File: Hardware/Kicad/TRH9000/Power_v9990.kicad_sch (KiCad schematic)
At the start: 21 parts, among them U1 V9990, U2 KM428C256, U3 KM428C256, U4 74VHC138, U6 LMH1980, U7 T.I_SN74AHCT32D

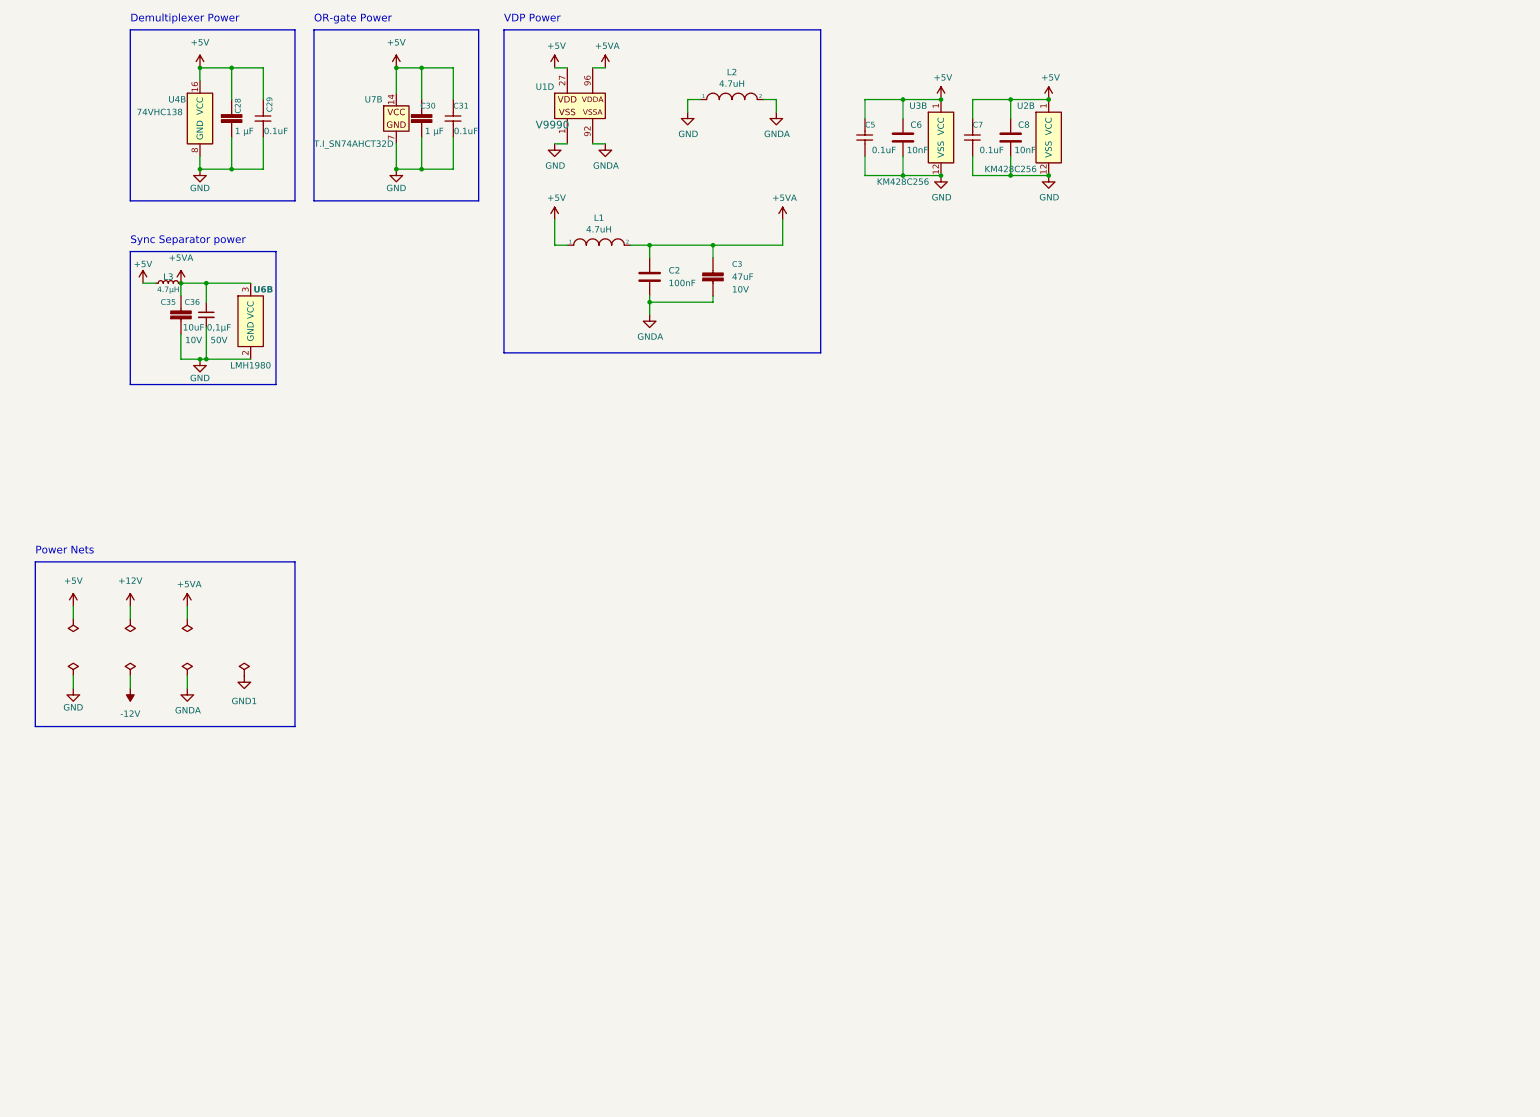
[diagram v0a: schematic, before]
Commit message: Started routing the PCB, adding cut-outs to separate the analog from digital signal-domains.
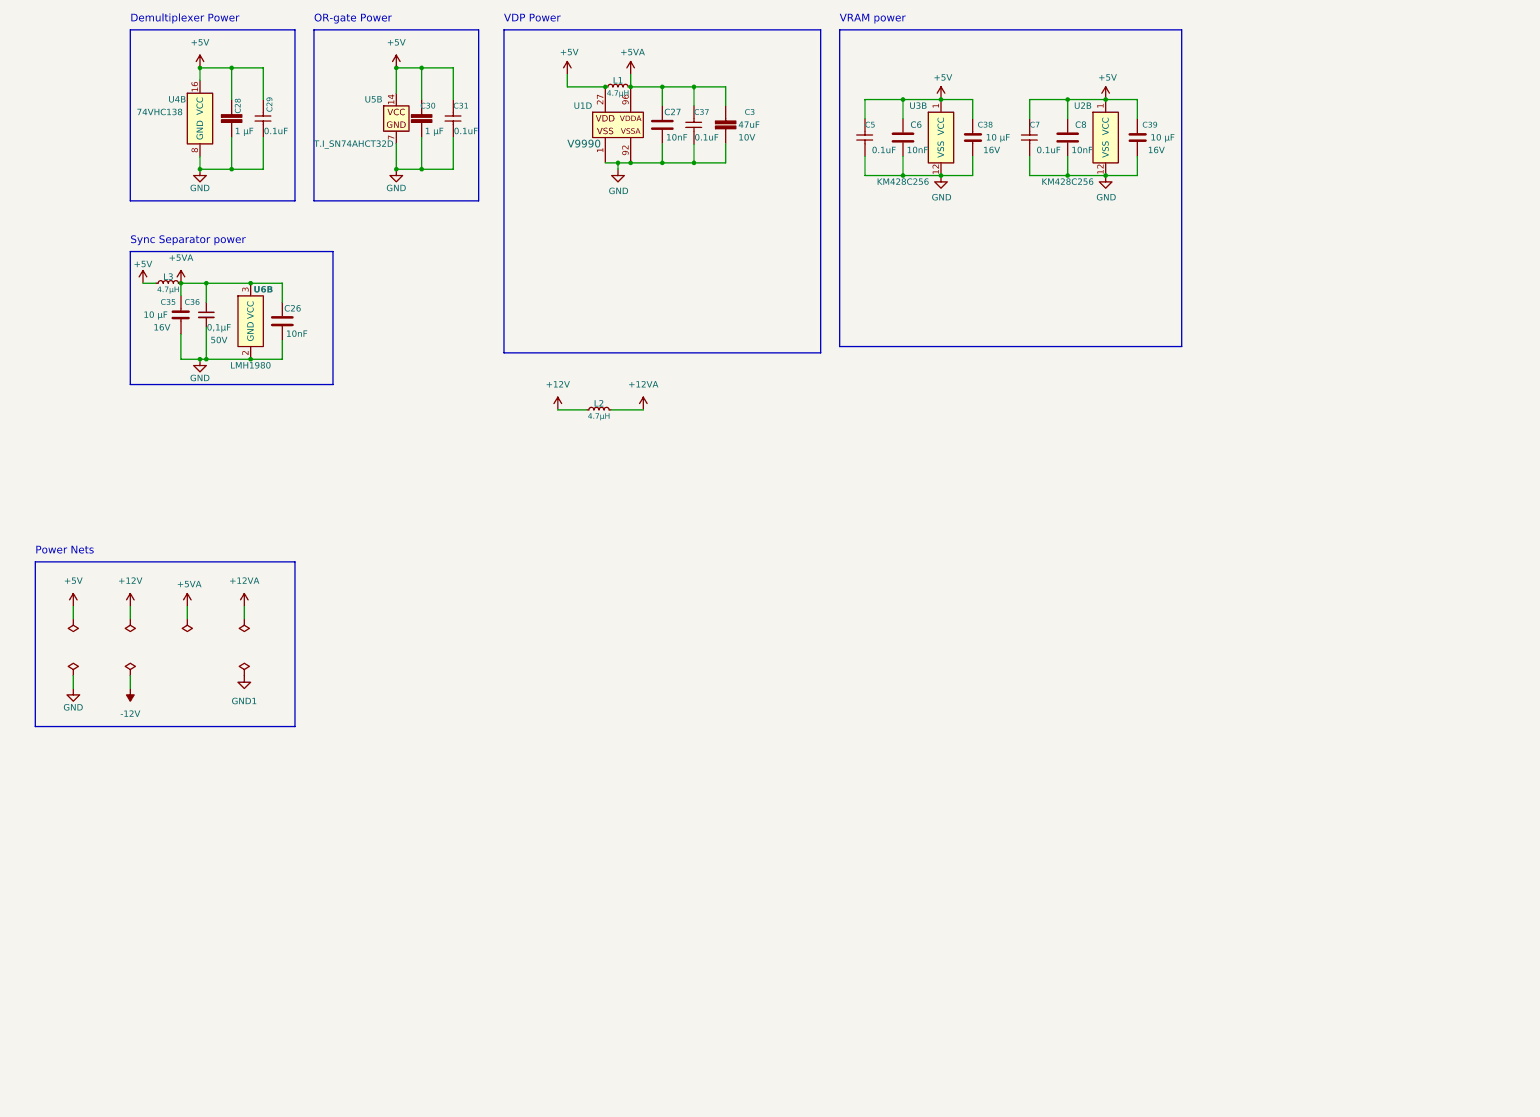
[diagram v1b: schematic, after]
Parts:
- removed C2: 100nF, Capacitor_SMD:C_0805_2012Metric, symbol Device:C
- removed L1, L2: 4.7uH, Inductor_SMD:L_1206_3216Metric, symbol pspice:INDUCTOR
- added C26, C27: 10nF, Capacitor_SMD:C_0805_2012Metric, symbol Device:C
- added C37: C_CC0805JPX7R9BB104, Capacitor_SMD:C_0805_2012Metric, symbol LRJ-parts:C_CC0805JPX7R9BB104
- added C38, C39: C_CL21B106KOQNNNE, Capacitor_SMD:C_0805_2012Metric, symbol LRJ-parts:C_CL21B106KOQNNNE
- added L1, L2: L_MLZ2012M4R7HT000, Inductor_SMD:L_0805_2012Metric, symbol LRJ-parts:L_MLZ2012M4R7HT000
- C35: value C_GRM21BR71A106KA73K -> C_CL21B106KOQNNNE; footprint Capacitor_SMD:C_0805_2012Metric_Pad1.18x1.45mm_HandSolder -> Capacitor_SMD:C_0805_2012Metric; symbol LRJ-parts:C_GRM21BR71A106KA73K -> LRJ-parts:C_CL21B106KOQNNNE;  Temperature Coefficient  X7R -> (none); Capacitance 10uF -> 10 µF; MPN GRM21BR71A106KA73K -> CL21B106KOQNNNE; Manufacturer Murata Electronics -> Samsung Electro-Mechanics; Mounting type (none) -> SMD; Status (none) -> Active; Temperature Coefficient  (none) -> X7R; Tolerance ±10% -> (none); Voltage rating 10V -> 16V
- renumbered U7 to U5
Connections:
- net GNDA is gone; now on net GND: C3.2, U1.92 (VSSA)
- net +12V: now also L2.1
- net +5V: now also C38.1, C39.1, L1.1
- net +5VA: now also C26.2, C27.2, C37.1, L1.2
- net GND: now also C26.1, C27.1, C37.2, C38.2, C39.2
- new net +12VA: L2.2
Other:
- note added: "VRAM power"
- moved on the sheet: C3, C7, C8, U1D, U2B

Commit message: More routing of the analog portion. Added 3D-models for the VGA and Scart connectors.
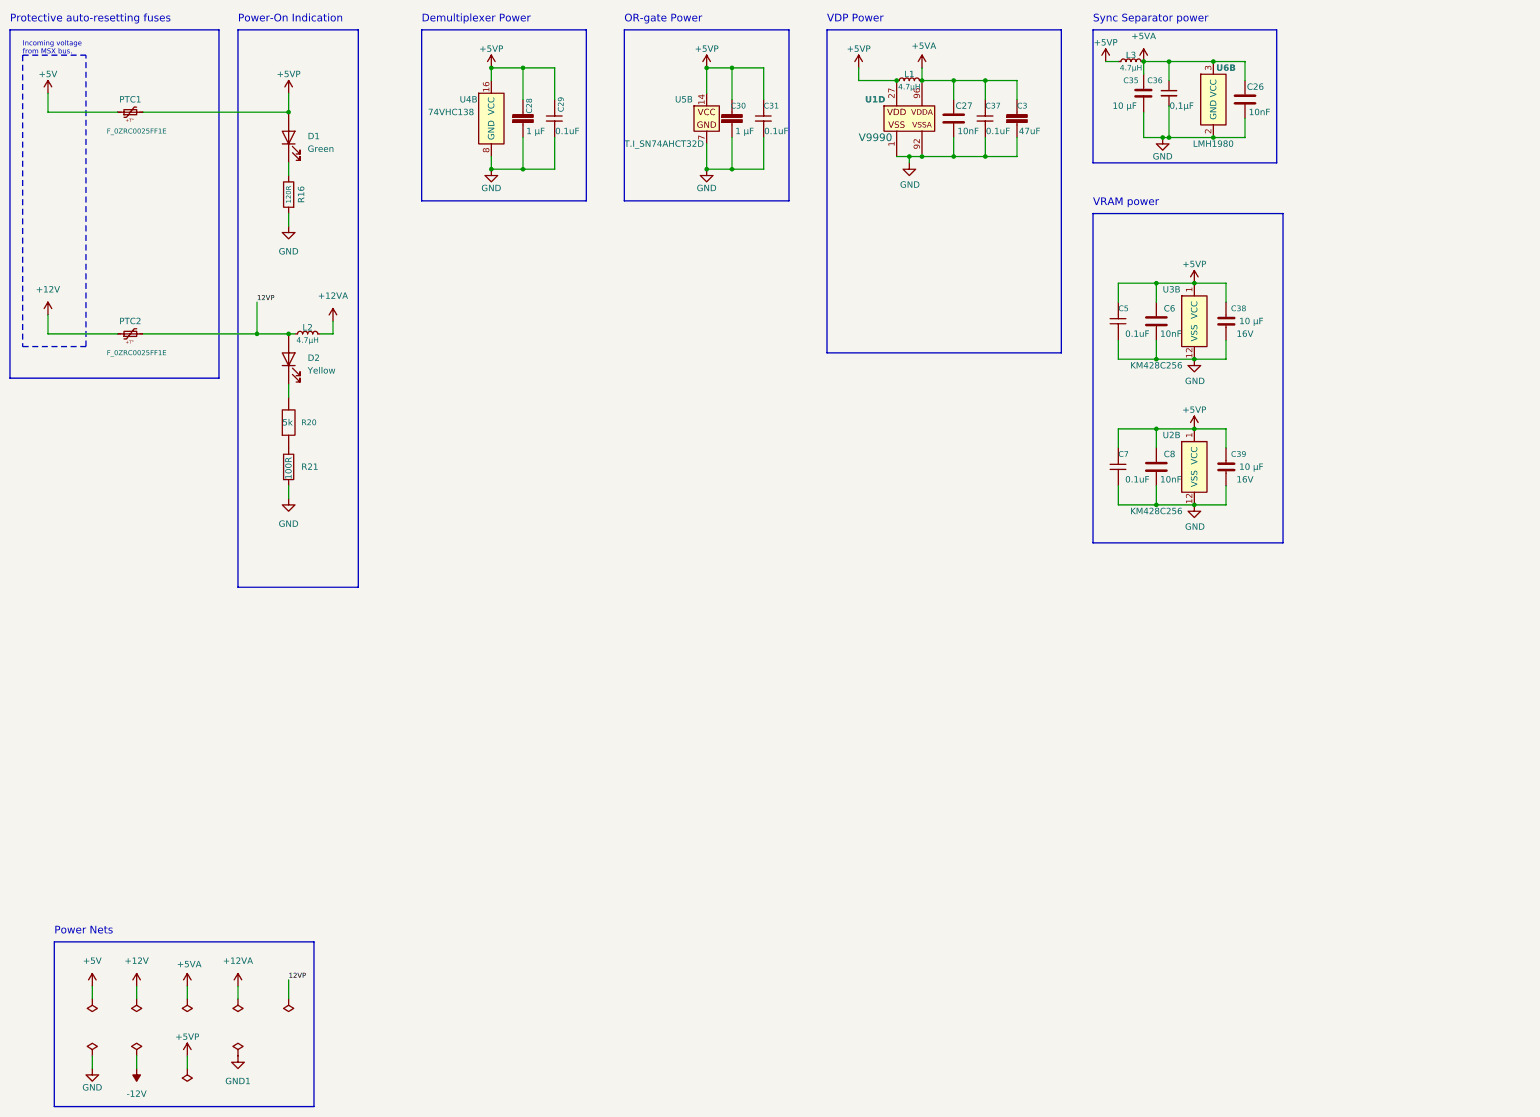
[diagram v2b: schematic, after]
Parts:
- added D1: SunLED_XCVG12D, LED_THT:LED_D5.0mm, symbol LRJ-parts:SunLED_XCVG12D
- added D2: LO_LED_LTL2R3K, LED_THT:LED_D5.0mm, symbol LRJ-parts:LO_LED_LTL2R3K
- added PTC1, PTC2: F_0ZRC0025FF1E, LRJ:Fuse_BelFuse_0ZRC0025FF_L7.4mm_W3.1mm, symbol LRJ-parts:F_0ZRC0025FF1E
- added R16: 120R, Resistor_SMD:R_0603_1608Metric, symbol Device:R
- added R20: R_RT0603BRE075KL, Resistor_SMD:R_0603_1608Metric_Pad0.98x0.95mm_HandSolder, symbol LRJ-parts:R_RT0603BRE075KL
- added R21: 100R, Resistor_SMD:R_0805_2012Metric, symbol Device:R
- C29, C31, C37, C5, C7: Price €0,14 -> (none)
- C3: Capacitance (none) -> 47uF; Capacity 47uF -> (none)
- C36: Mounting Type SMD -> (none); Voltage Rating (none) -> 50V; Voltage Rating  50V -> (none)
- U1: Status (none) -> OBSOLETE
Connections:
- net +12V: now also PTC2.1; no longer L2.1
- net +5V: now also PTC1.1; no longer C28.1, C29.1, C30.1, C31.1, C38.1, C39.1, C5.1, C6.2, C7.1, C8.2, L1.1, L3.1, U1.123 (VDD), U1.27 (VDD), U1.53 (VDD), U1.81 (VDD), U1.97 (VDD), U2.1 (VCC), U2.20 (VCC), U3.1 (VCC), U3.20 (VCC), U4.16 (VCC), U5.14 (VCC)
- net GND: now also R16.2, R21.2
- new net: D1.1 (K), R16.1
- new net: R20.1, R21.1
- new net: D2.1 (K), R20.2
- new net +5VP: C28.1, C29.1, C30.1, C31.1, C38.1, C39.1, C5.1, C6.2, C7.1, C8.2, D1.2 (A), L1.1, L3.1, PTC1.2, U1.123 (VDD), U1.27 (VDD), U1.53 (VDD), U1.81 (VDD), U1.97 (VDD), U2.1 (VCC), U2.20 (VCC), U3.1 (VCC), U3.20 (VCC), U4.16 (VCC), U5.14 (VCC)
- new net 12VP: D2.2 (A), L2.1, PTC2.2
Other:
- note added: "Incoming voltage from MSX bus."
- note added: "Power-On Indication"
- note added: "Protective auto-resetting fuses"
- company: (none) -> The Retro Hacker
- title: (none) -> TRH9000
- moved on the sheet: C26, C27, C28, C29, C3, C30, C31, C35, C36, C37, C38, C39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

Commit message: Did a reroute of the analog / digital separation.
Did a reroute of the analog / digital separation.
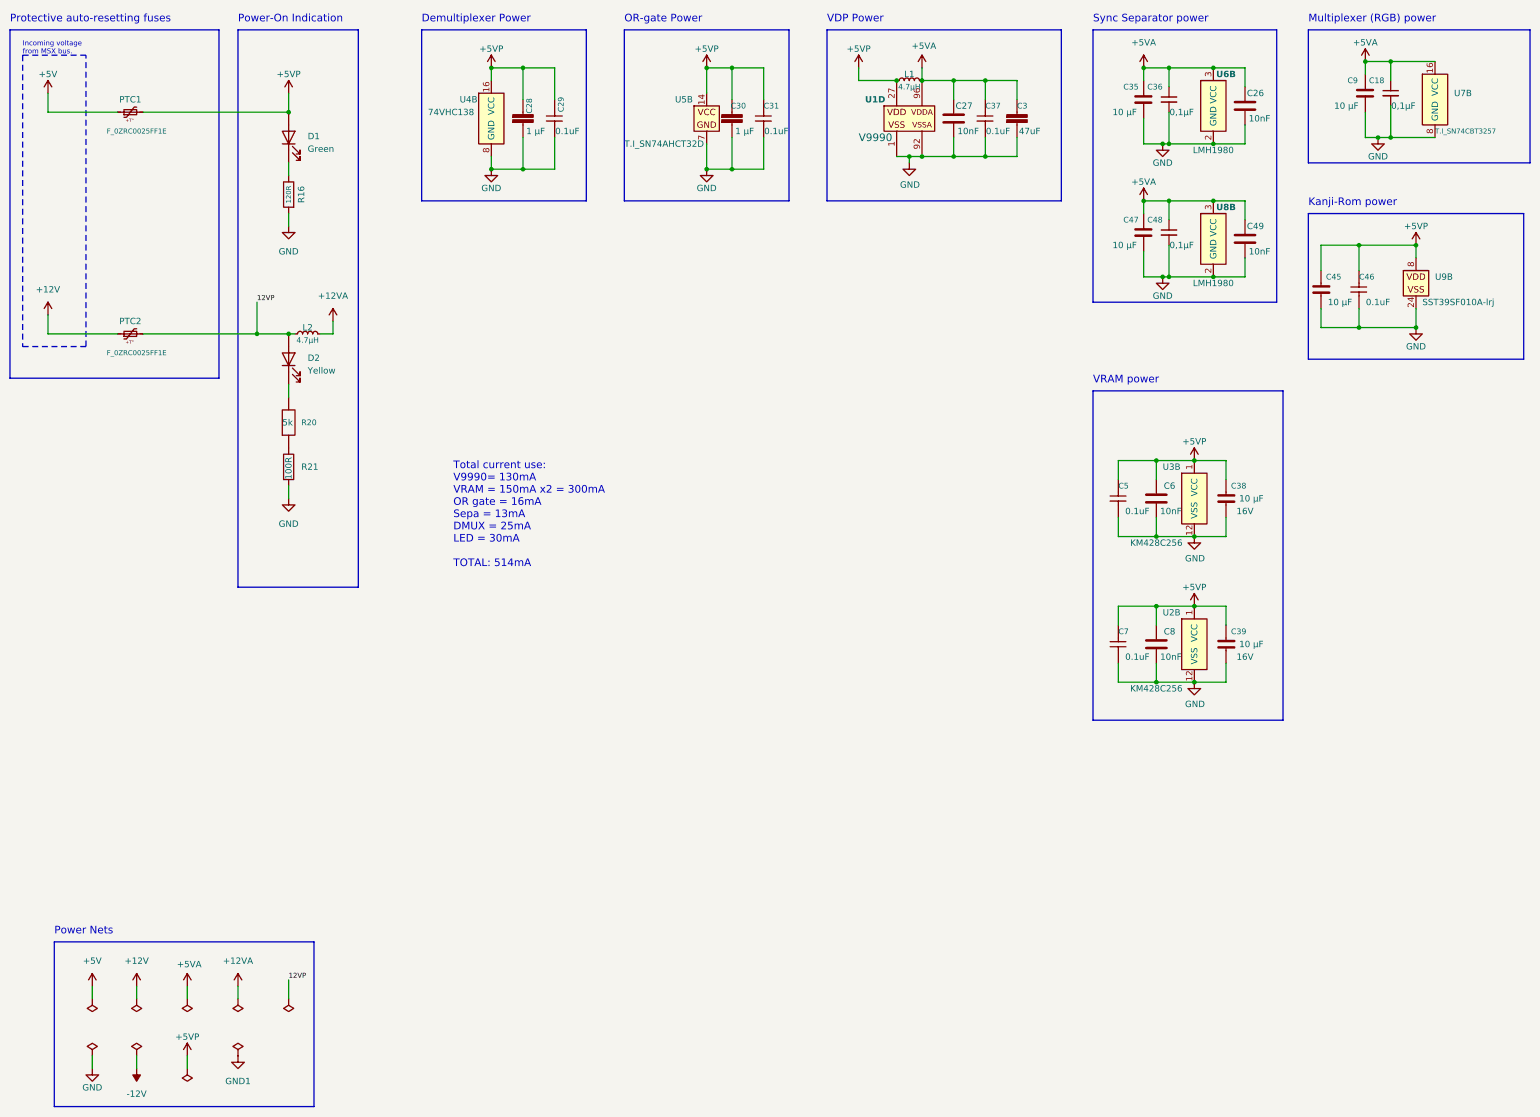
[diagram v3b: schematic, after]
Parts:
- removed L3: L_MLZ2012M4R7HT000, Inductor_SMD:L_0805_2012Metric, symbol LRJ-parts:L_MLZ2012M4R7HT000
- added C18, C48: C_CL10B104KB8NNNL, Capacitor_SMD:C_0603_1608Metric_Pad1.08x0.95mm_HandSolder, symbol LRJ-parts:C_CL10B104KB8NNNL
- added C45, C47, C9: C_CL21B106KOQNNNE, Capacitor_SMD:C_0805_2012Metric, symbol LRJ-parts:C_CL21B106KOQNNNE
- added C46: C_CC0805JPX7R9BB104, Capacitor_SMD:C_0805_2012Metric, symbol LRJ-parts:C_CC0805JPX7R9BB104
- added C49: 10nF, Capacitor_SMD:C_0805_2012Metric, symbol Device:C
- added U7: T.I_SN74CBT3257, trh9000:Texas_R-PDSO-G16_3.9x9.9mm, symbol TRH9000:T.I_SN74CBT3257
- added U8: LMH1980, Package_SO:VSSOP-10_3x3mm_P0.5mm, symbol LRJ-parts:LMH1980
- added U9: SST39SF010A-lrj, Package_SO:TSOP-I-32_12.4x8mm_P0.5mm, symbol LRJ-parts:SST39SF010A-lrj
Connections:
- net +5VA: now also C18.1, C47.1, C48.1, C49.2, C9.1, U7.16 (VCC), U8.3 (VCC)
- net +5VP: now also C45.1, C46.1, U9.8 (VDD)
- net GND: now also C18.2, C45.2, C46.2, C47.2, C48.2, C49.1, C9.2, U7.8 (GND), U8.2 (GND), U9.24 (VSS)
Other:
- note added: "Kanji-Rom power"
- note added: "Multiplexer (RGB) power"
- note added: "Total current use: V9990= 130mA VRAM = 150mA x2 = 300mA OR gate = 16mA Sepa = 13mA DMUX = 25mA LED = 30mA TOTAL: 514mA"
- moved on the sheet: C26, C35, C36, C38, C39, C5, C6, C7, C8, U2B, U3B, U6B
